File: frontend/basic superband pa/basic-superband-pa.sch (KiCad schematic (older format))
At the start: 63 parts, among them CN1 EDGE, K1 D3002, K2 D3002, P1 BNC, P2 CONN_02X01, Q1 FDV301, Q2 FDV301, Q3 RD16HHF1, T1 TRANSFO, T2 8:1, T3 4:1, T4 OUT_TRANSF, U1 LP2951-50D

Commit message: Added opto and change of PTT
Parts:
- removed C1, C25, C27: 0.01uF, HERMESLITE:C_0805, symbol C
- removed Q1, Q2: FDV301, SMD_Packages:SOT-23-GDS, symbol MOS_N
- added C30, C31: 0.1uF, HERMESLITE:C_0805, symbol C
- added R1, R2: 1.2k, Resistors_SMD:R_0805_HandSoldering, symbol R
- added U2: LVT827, Power_Integrations:SMD-8, symbol PC827
- C22: footprint Capacitors_SMD:C_1206 -> Capacitors_Tantalum_SMD:TantalC_SizeC_EIA-6032_HandSoldering
- C7: footprint Discret:C1V8 -> Capacitors_Tantalum_SMD:TantalC_SizeD_EIA-7343_HandSoldering
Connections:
- net labels added: USEROUT0
- net labels removed: GPIO0
- wire segments 153 -> 155

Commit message: Second pass of superband
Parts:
- added D1: YEL LED (Band1), LEDs:LED-0805, symbol LED
- added D2: RED LED (PTT), LEDs:LED-0805, symbol LED
- added D3: GRN LED (PWR ON), LEDs:LED-0805, symbol LED
- added R13, R3, R9: 4.99k, Resistors_SMD:R_0805_HandSoldering, symbol R
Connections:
- net /PTT: now also R9.1
- net GND: now also R13.1
- net at C17.1, C26.2, C30.1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: now also D1.1 (A), D2.1 (A), D3.1 (A)
- net USEROUT4: now reaches CN1.B16 (USEROUT4)
- net USEROUT4: now also U2.3
- net BAND1: now reaches K1.10 (-), U2.6
- net BAND1: now also R3.1
- net USEROUT0: no longer names the net of CN1.B12 (USEROUT0)
- net USEROUT0: no longer U2.3
- new net: D2.2 (K), R9.2
- new net: D3.2 (K), R13.2
- new net: D1.2 (K), R3.2
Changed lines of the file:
@@
 $EndComp
 Text GLabel 1850 5650 0    60   Input ~ 0
-USEROUT0
+USEROUT4
 Text GLabel 3900 1350 2    60   Output ~ 0
-USEROUT0
+USEROUT4
 $Comp
 L INDUCTOR L7
@@
 	1750 4000 1600 4000
 Connection ~ 1600 4000
-Wire Wire Line
-	3550 2850 2950 2850
 Wire Wire Line
 	3650 3000 2950 3000
@@
 Connection ~ 4200 1650
 Connection ~ 4200 2150
-Connection ~ 2950 2850
 Connection ~ 2950 3000
 Connection ~ 2950 3100
@@
 Connection ~ 1750 4000
 Connection ~ 3800 1650
-Connection ~ 3100 4850
 Wire Wire Line
 	1550 1650 3800 1650
@@
 	5850 6200 6200 6200
 Wire Wire Line
-	6600 2350 6350 2350
-Wire Wire Line
-	6350 2350 6350 1550
+	6350 2350 6600 2350
 Connection ~ 6350 1550
 Wire Wire Line
@@
 	2300 6400 2950 6400
 Wire Wire Line
-	3550 2850 3550 1350
-Wire Wire Line
 	3650 1450 3650 3000
 NoConn ~ 1750 2350
@@
 NoConn ~ 2950 2250
 NoConn ~ 2950 2350
-NoConn ~ 2950 2450
 NoConn ~ 2950 2550
 NoConn ~ 2950 2650
@@
 F 0 "U2" H 2860 4890 40  0000 C CNN
 F 1 "LVT827" H 3210 4510 40  0000 C CNN
-F 2 "Power_Integrations:SMD-8" H 2850 4520 30  0000 C CIN
+F 2 "Power_Integrations:SMD-8" H 2850 4520 30  0001 C CIN
 F 3 "" H 3050 4700 60  0000 C CNN
 	1    3050 4700
@@
 	1500 5850 1600 5850
 Wire Wire Line
-	2800 5650 2950 5650
-Wire Wire Line
-	2950 5650 2950 6400
+	2800 5650 3150 5650
+Wire Wire Line
+	2950 6400 2950 5650
 Wire Wire Line
 	1850 5650 2100 5650
@@
 Connection ~ 4500 1950
 Connection ~ 4750 1950
+NoConn ~ 2950 2850
+Wire Wire Line
+	2950 2450 3550 2450
+Wire Wire Line
+	3550 2450 3550 1350
+$Comp
+L LED D2
+U 1 1 54E899BF
+P 6350 900
+F 0 "D2" H 6350 1000 50  0000 C CNN
+F 1 "RED LED (PTT)" H 6350 800 40  0000 C CNN
+F 2 "LEDs:LED-0805" H 6350 900 60  0001 C CNN
+F 3 "" H 6350 900 60  0000 C CNN
+	1    6350 900
+	1    0    0    -1
+$EndComp
+Text GLabel 3150 5650 2    50   Output ~ 0
+BAND1
+Connection ~ 2950 5650
+$Comp
+L LED D3
+U 1 1 54E8AC32
+P 6950 1100
+F 0 "D3" H 6950 1200 50  0000 C CNN
+F 1 "GRN LED (PWR ON)" H 6950 1000 40  0000 C CNN
+F 2 "LEDs:LED-0805" H 6950 1100 60  0001 C CNN
+F 3 "" H 6950 1100 60  0000 C CNN
+	1    6950 1100
+	1    0    0    -1
+$EndComp
+$Comp
+L LED D1
+U 1 1 54E8AC8C
+P 5750 700
+F 0 "D1" H 5750 800 50  0000 C CNN
+F 1 "YEL LED (Band1)" H 5750 600 40  0000 C CNN
+F 2 "LEDs:LED-0805" H 5750 700 60  0001 C CNN
+F 3 "" H 5750 700 60  0000 C CNN
+	1    5750 700
+	1    0    0    -1
+$EndComp
+Wire Wire Line
+	5250 1100 6750 1100
+$Comp
+L R R13
+U 1 1 54E8B1B0
+P 7400 1100
+F 0 "R13" V 7480 1100 40  0000 C CNN
+F 1 "4.99k" V 7407 1101 40  0000 C CNN
+F 2 "Resistors_SMD:R_0805_HandSoldering" V 7330 1100 30  0001 C CNN
+F 3 "" H 7400 1100 30  0000 C CNN
+	1    7400 1100
+	0    1    1    0
+$EndComp
+$Comp
+L R R9
+U 1 1 54E8B2ED
+P 6800 900
+F 0 "R9" V 6880 900 40  0000 C CNN
+F 1 "4.99k" V 6807 901 40  0000 C CNN
+F 2 "Resistors_SMD:R_0805_HandSoldering" V 6730 900 30  0001 C CNN
+F 3 "" H 6800 900 30  0000 C CNN
+	1    6800 900
+	0    1    1    0
+$EndComp
+$Comp
+L R R3
+U 1 1 54E8B399
+P 6200 700
+F 0 "R3" V 6280 700 40  0000 C CNN
+F 1 "4.99k" V 6207 701 40  0000 C CNN
+F 2 "Resistors_SMD:R_0805_HandSoldering" V 6130 700 30  0001 C CNN
+F 3 "" H 6200 700 30  0000 C CNN
+	1    6200 700
+	0    1    1    0
+$EndComp
+Wire Wire Line
+	5250 1550 5250 700
+Wire Wire Line
+	5250 700  5550 700
+Wire Wire Line
+	5250 900  6150 900
+Connection ~ 5250 900
+Wire Wire Line
+	6350 1550 6350 2350
+Connection ~ 5250 1100
+Wire Wire Line
+	7650 1100 7750 1100
+Wire Wire Line
+	7750 1100 7750 1200
+$Comp
+L GND #PWR036
+U 1 1 54E8C475
+P 7750 1200
+F 0 "#PWR036" H 7750 1200 30  0001 C CNN
+F 1 "GND" H 7750 1130 30  0001 C CNN
+F 2 "" H 7750 1200 60  0000 C CNN
+F 3 "" H 7750 1200 60  0000 C CNN
+	1    7750 1200
+	1    0    0    -1
+$EndComp
+Text GLabel 7200 900  2    50   Input ~ 0
+/PTT
+Text GLabel 6600 700  2    50   Input ~ 0
+BAND1
+Wire Wire Line
+	6450 700  6600 700
+Wire Wire Line
+	7050 900  7200 900
 $EndSCHEMATC

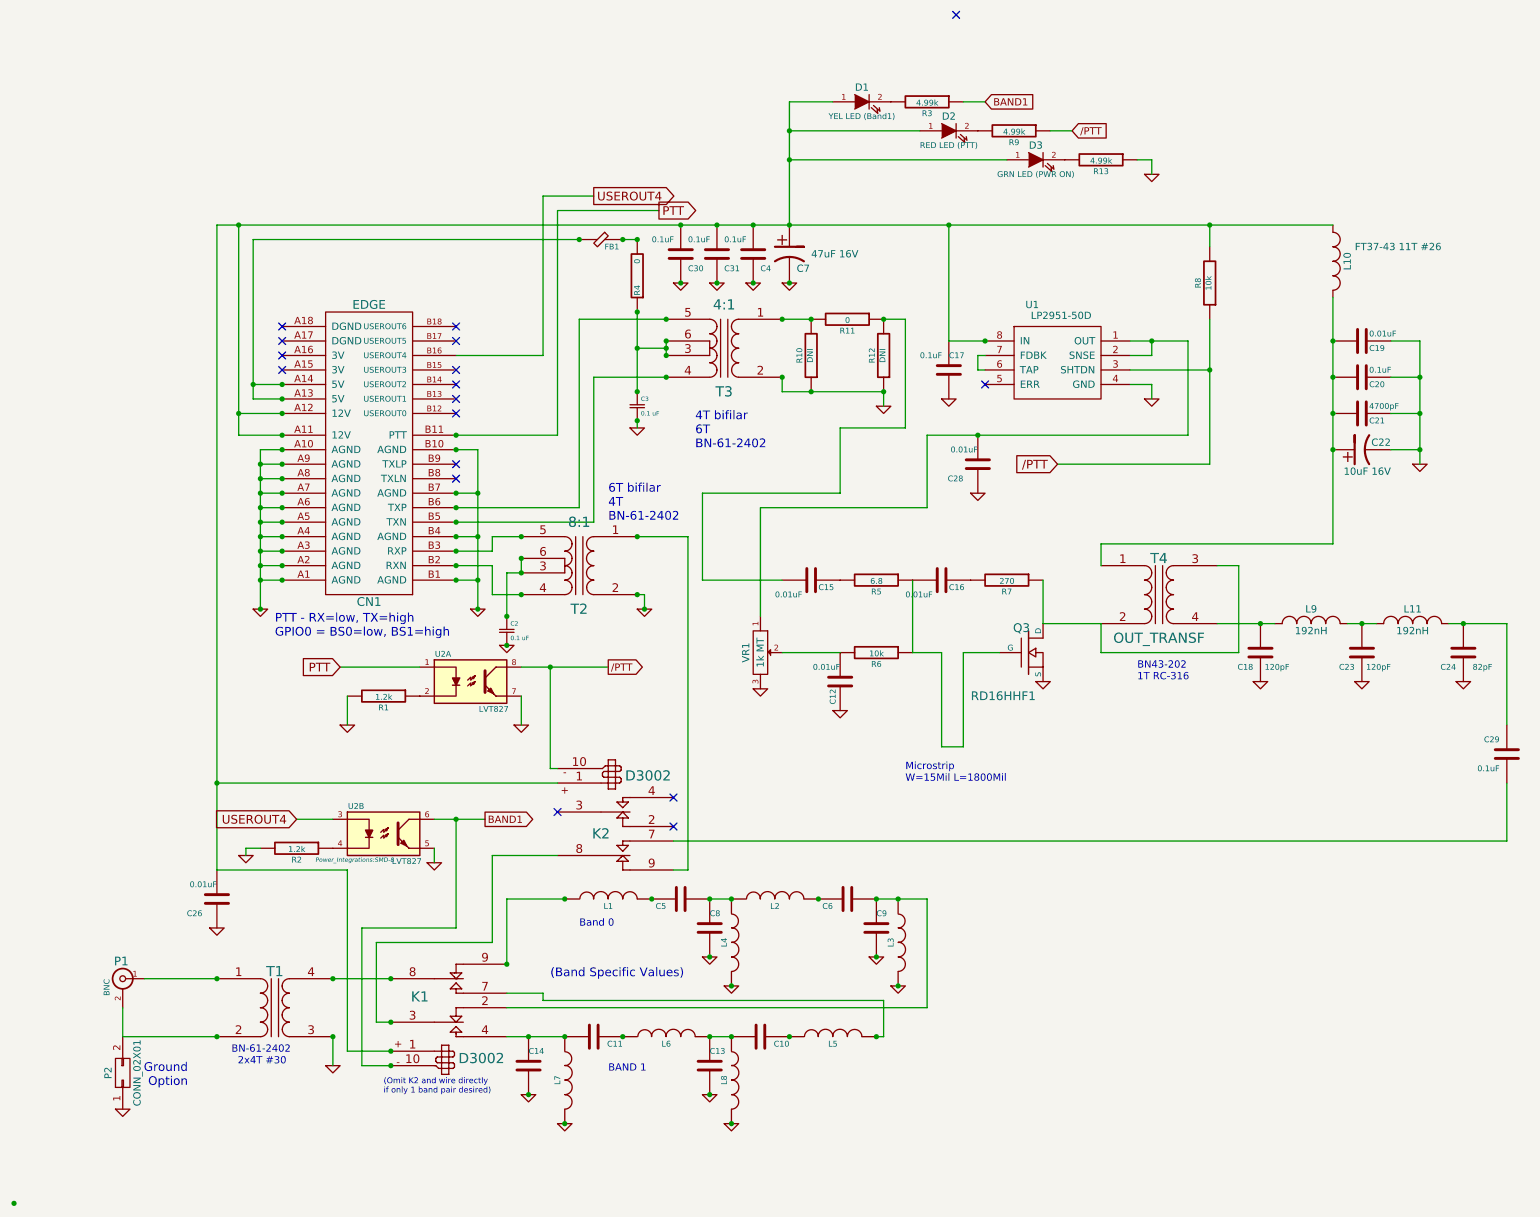
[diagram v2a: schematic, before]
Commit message: modify mounting holes
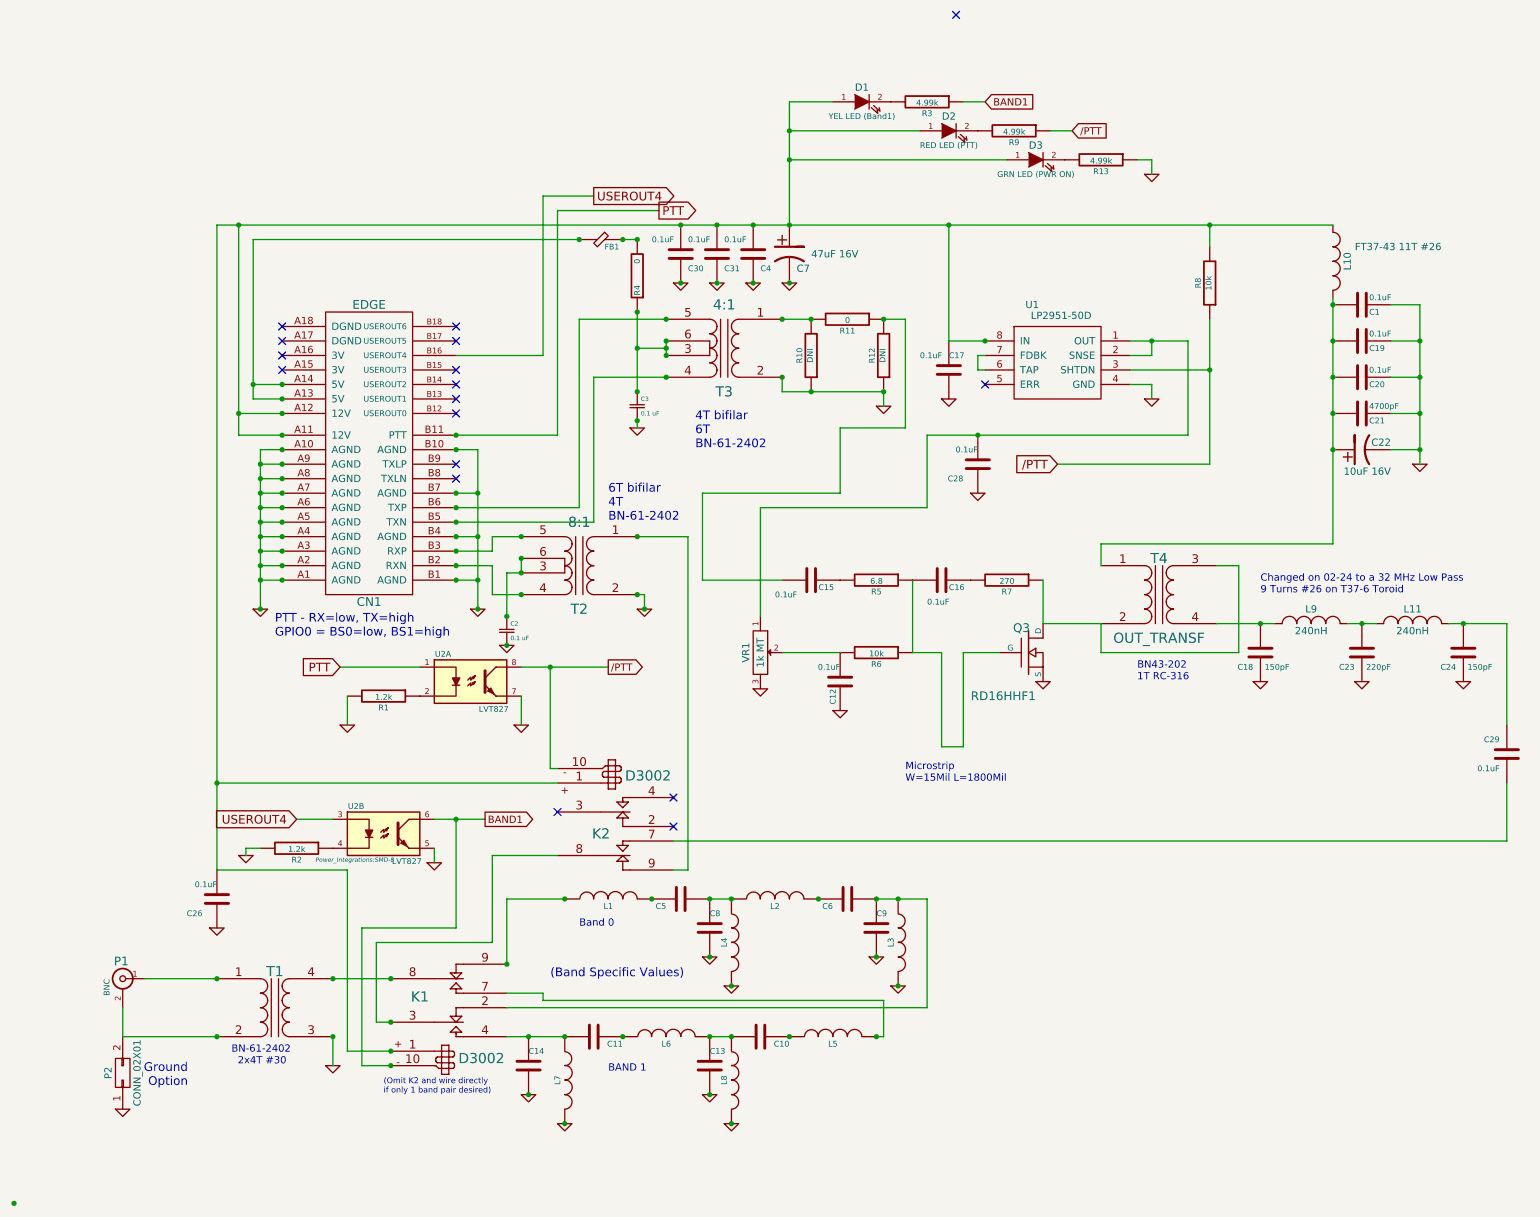
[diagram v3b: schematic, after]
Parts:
- added C1: 0.1uF, HERMESLITE:C_0805, symbol C
- C12, C15, C16, C19, C26, C28: value 0.01uF -> 0.1uF
- C18: value 120pF -> 150pF
- C23: value 120pF -> 220pF
- C24: value 82pF -> 150pF
- L11, L9: value 192nH -> 240nH
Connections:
- net GND: now also C1.1
- net at C19.2, C20.2, C21.2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: now also C1.2
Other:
- note added: "Changed on 02-24 to a 32 MHz Low Pass\n9 Turns #26 on T37-6 Toroid"
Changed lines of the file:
@@
 Sheet 1 1
 Title "Hermes-Lite Basic Superband 5W Power Amplifier"
-Date "15 January 2015"
-Rev "1.0"
+Date "10 March 2015"
+Rev "1.1"
 Comp "SofterHardware"
 Comment1 "AC9HY"
@@
 P 5400 4000
 F 0 "C15" V 5450 4050 40  0000 L CNN
-F 1 "0.01uF" V 5500 3750 40  0000 L CNN
+F 1 "0.1uF" V 5500 3750 40  0000 L CNN
 F 2 "HERMESLITE:C_0805" H 5438 3850 30  0001 C CNN
 F 3 "" H 5400 4000 60  0000 C CNN
@@
 P 6300 4000
 F 0 "C16" V 6350 4050 40  0000 L CNN
-F 1 "0.01uF" V 6400 3750 40  0000 L CNN
+F 1 "0.1uF" V 6450 3900 40  0000 L CNN
 F 2 "HERMESLITE:C_0805" H 6338 3850 30  0001 C CNN
 F 3 "" H 6300 4000 60  0000 C CNN
@@
 P 5600 4700
 F 0 "C12" V 5650 4750 40  0000 L CNN
-F 1 "0.01uF" H 5600 4600 40  0000 L CNN
+F 1 "0.1uF" H 5600 4600 40  0000 L CNN
 F 2 "HERMESLITE:C_0805" H 5638 4550 30  0001 C CNN
 F 3 "" H 5600 4700 60  0000 C CNN
@@
 P 8500 4500
 F 0 "C18" H 8550 4600 40  0000 L CNN
-F 1 "120pF" H 8300 4600 40  0000 L CNN
+F 1 "150pF" H 8300 4600 40  0000 L CNN
 F 2 "HERMESLITE:C_0805" H 8538 4350 30  0001 C CNN
 F 3 "" H 8500 4500 60  0000 C CNN
@@
 P 9200 2350
 F 0 "C19" V 9250 2400 40  0000 L CNN
-F 1 "0.01uF" V 9150 2400 40  0000 L CNN
+F 1 "0.1uF" V 9150 2400 40  0000 L CNN
 F 2 "HERMESLITE:C_0805" H 9238 2200 30  0001 C CNN
 F 3 "" H 9200 2350 60  0000 C CNN
@@
 P 8850 4300
 F 0 "L9" H 8850 4400 50  0000 C CNN
-F 1 "192nH" H 8850 4250 50  0000 C CNN
+F 1 "240nH" H 8850 4250 50  0000 C CNN
 F 2 "Choke_Toroid_ThroughHole:Choke_Toroid_6,5x13mm_Vertical" H 8850 4300 60  0001 C CNN
 F 3 "" H 8850 4300 60  0000 C CNN
@@
 P 9550 4300
 F 0 "L11" H 9550 4400 50  0000 C CNN
-F 1 "192nH" H 9550 4250 50  0000 C CNN
+F 1 "240nH" H 9550 4250 50  0000 C CNN
 F 2 "Choke_Toroid_ThroughHole:Choke_Toroid_6,5x13mm_Vertical" H 9550 4300 60  0001 C CNN
 F 3 "" H 9550 4300 60  0000 C CNN
@@
 P 9200 4500
 F 0 "C23" H 9250 4600 40  0000 L CNN
-F 1 "120pF" H 9000 4600 40  0000 L CNN
+F 1 "220pF" H 9000 4600 40  0000 L CNN
 F 2 "HERMESLITE:C_0805" H 9238 4350 30  0001 C CNN
 F 3 "" H 9200 4500 60  0000 C CNN
@@
 P 9900 4500
 F 0 "C24" H 9950 4600 40  0000 L CNN
-F 1 "82pF" H 9700 4600 40  0000 L CNN
+F 1 "150pF" H 9700 4600 40  0000 L CNN
 F 2 "HERMESLITE:C_0805" H 9938 4350 30  0001 C CNN
 F 3 "" H 9900 4500 60  0000 C CNN
@@
 	9400 2350 9600 2350
 Wire Wire Line
-	9600 2350 9600 3200
+	9600 2100 9600 3200
 Wire Wire Line
 	9400 3100 9600 3100
@@
 P 6550 3200
 F 0 "C28" H 6650 3300 40  0000 L CNN
-F 1 "0.01uF" H 6550 3100 40  0000 L CNN
+F 1 "0.1uF" H 6550 3100 40  0000 L CNN
 F 2 "HERMESLITE:C_0805" H 6588 3050 30  0001 C CNN
 F 3 "" H 6550 3200 60  0000 C CNN
@@
 P 1300 6200
 F 0 "C26" H 1400 6300 40  0000 L CNN
-F 1 "0.01uF" H 1300 6100 40  0000 L CNN
+F 1 "0.1uF" H 1300 6100 40  0000 L CNN
 F 2 "HERMESLITE:C_0805" H 1338 6050 30  0001 C CNN
 F 3 "" H 1300 6200 60  0000 C CNN
@@
 Wire Wire Line
 	7050 900  7200 900
+Text Notes 8500 4100 0    50   ~ 0
+Changed on 02-24 to a 32 MHz Low Pass\n9 Turns #26 on T37-6 Toroid
+$Comp
+L C C1
+U 1 1 54ED3E64
+P 9200 2100
+F 0 "C1" V 9250 2150 40  0000 L CNN
+F 1 "0.1uF" V 9150 2150 40  0000 L CNN
+F 2 "HERMESLITE:C_0805" H 9238 1950 30  0001 C CNN
+F 3 "" H 9200 2100 60  0000 C CNN
+	1    9200 2100
+	0    1    1    0
+$EndComp
+Connection ~ 9000 2100
+Wire Wire Line
+	9400 2100 9600 2100
+Connection ~ 9600 2350
 $EndSCHEMATC
